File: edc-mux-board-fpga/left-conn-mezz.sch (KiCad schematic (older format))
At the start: 86 parts, among them J13 Device 0, J14 Device 3, J15 Device 1, J16 Device 4, J17 Left Mezzanine Board Connecto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, J18 Left Mezzanine Board Connecto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, J19 Device 2, J20 Device 5

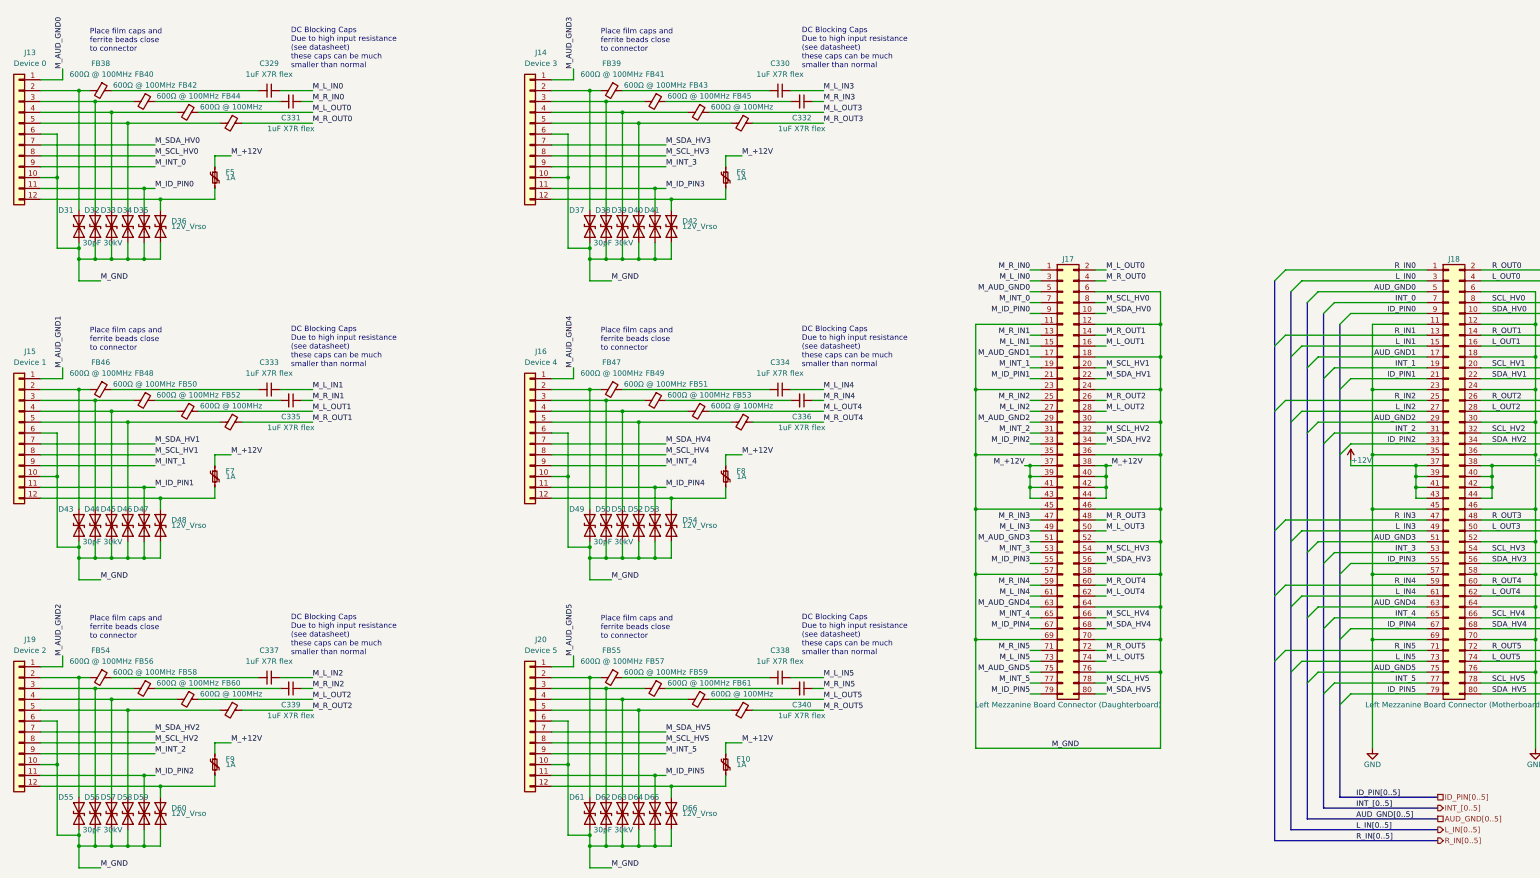
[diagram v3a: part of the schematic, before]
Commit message: re-annotating after adding power ICs and decoupling capacitors.
Also verified most footprints, and updated schematic field data.
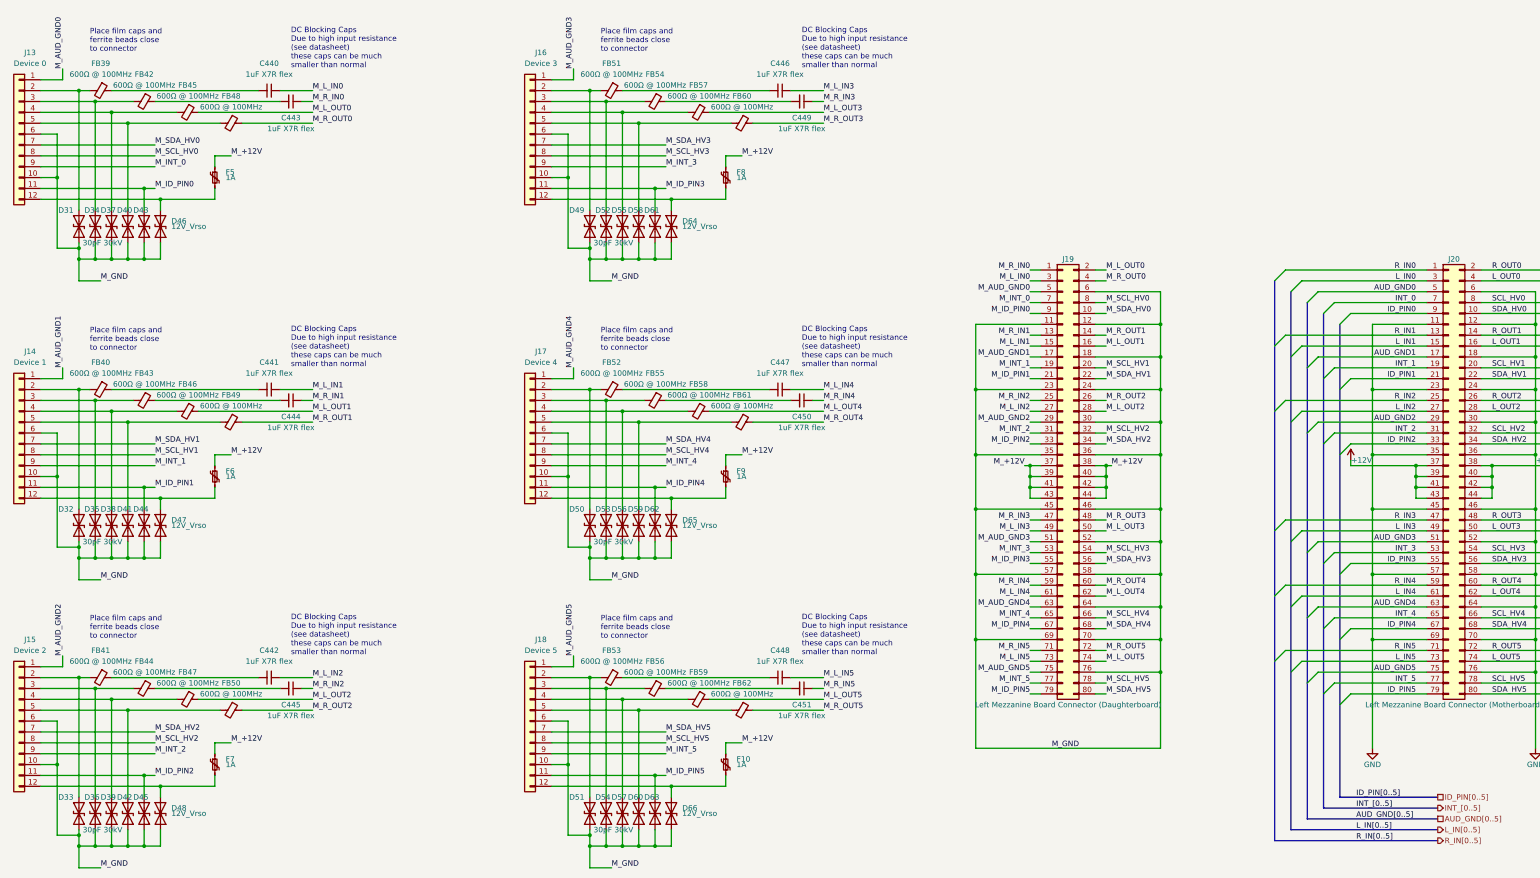
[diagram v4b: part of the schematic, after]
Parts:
- renumbered C329 to C440, C333 to C441, C337 to C442, C331 to C443, C335 to C444, C339 to C445, C330 to C446, C334 to C447, C338 to C448, C332 to C449, C336 to C450, C340 to C451, D43 to D32, D55 to D33, D32 to D34, D44 to D35, D56 to D36, D33 to D37, D45 to D38, D57 to D39, D34 to D40, D46 to D41, D58 to D42, D35 to D43, D47 to D44, D59 to D45, D36 to D46, D48 to D47, D60 to D48, D37 to D49, D49 to D50, D61 to D51, D38 to D52, D50 to D53, D62 to D54, D39 to D55, D51 to D56, D63 to D57, D40 to D58, D52 to D59, D64 to D60, D41 to D61, D53 to D62, D65 to D63, D42 to D64, D54 to D65, F7 to F6, F9 to F7, F6 to F8, F8 to F9, FB38 to FB39, FB46 to FB40, FB54 to FB41, FB40 to FB42, FB48 to FB43, FB56 to FB44, FB42 to FB45, FB50 to FB46, FB58 to FB47, FB44 to FB48, FB52 to FB49, FB60 to FB50, FB39 to FB51, FB47 to FB52, FB55 to FB53, FB41 to FB54, FB49 to FB55, FB57 to FB56, FB43 to FB57, FB51 to FB58, FB45 to FB60, FB53 to FB61, FB61 to FB62, J15 to J14, J19 to J15, J14 to J16, J16 to J17, J20 to J18, J17 to J19, J18 to J20

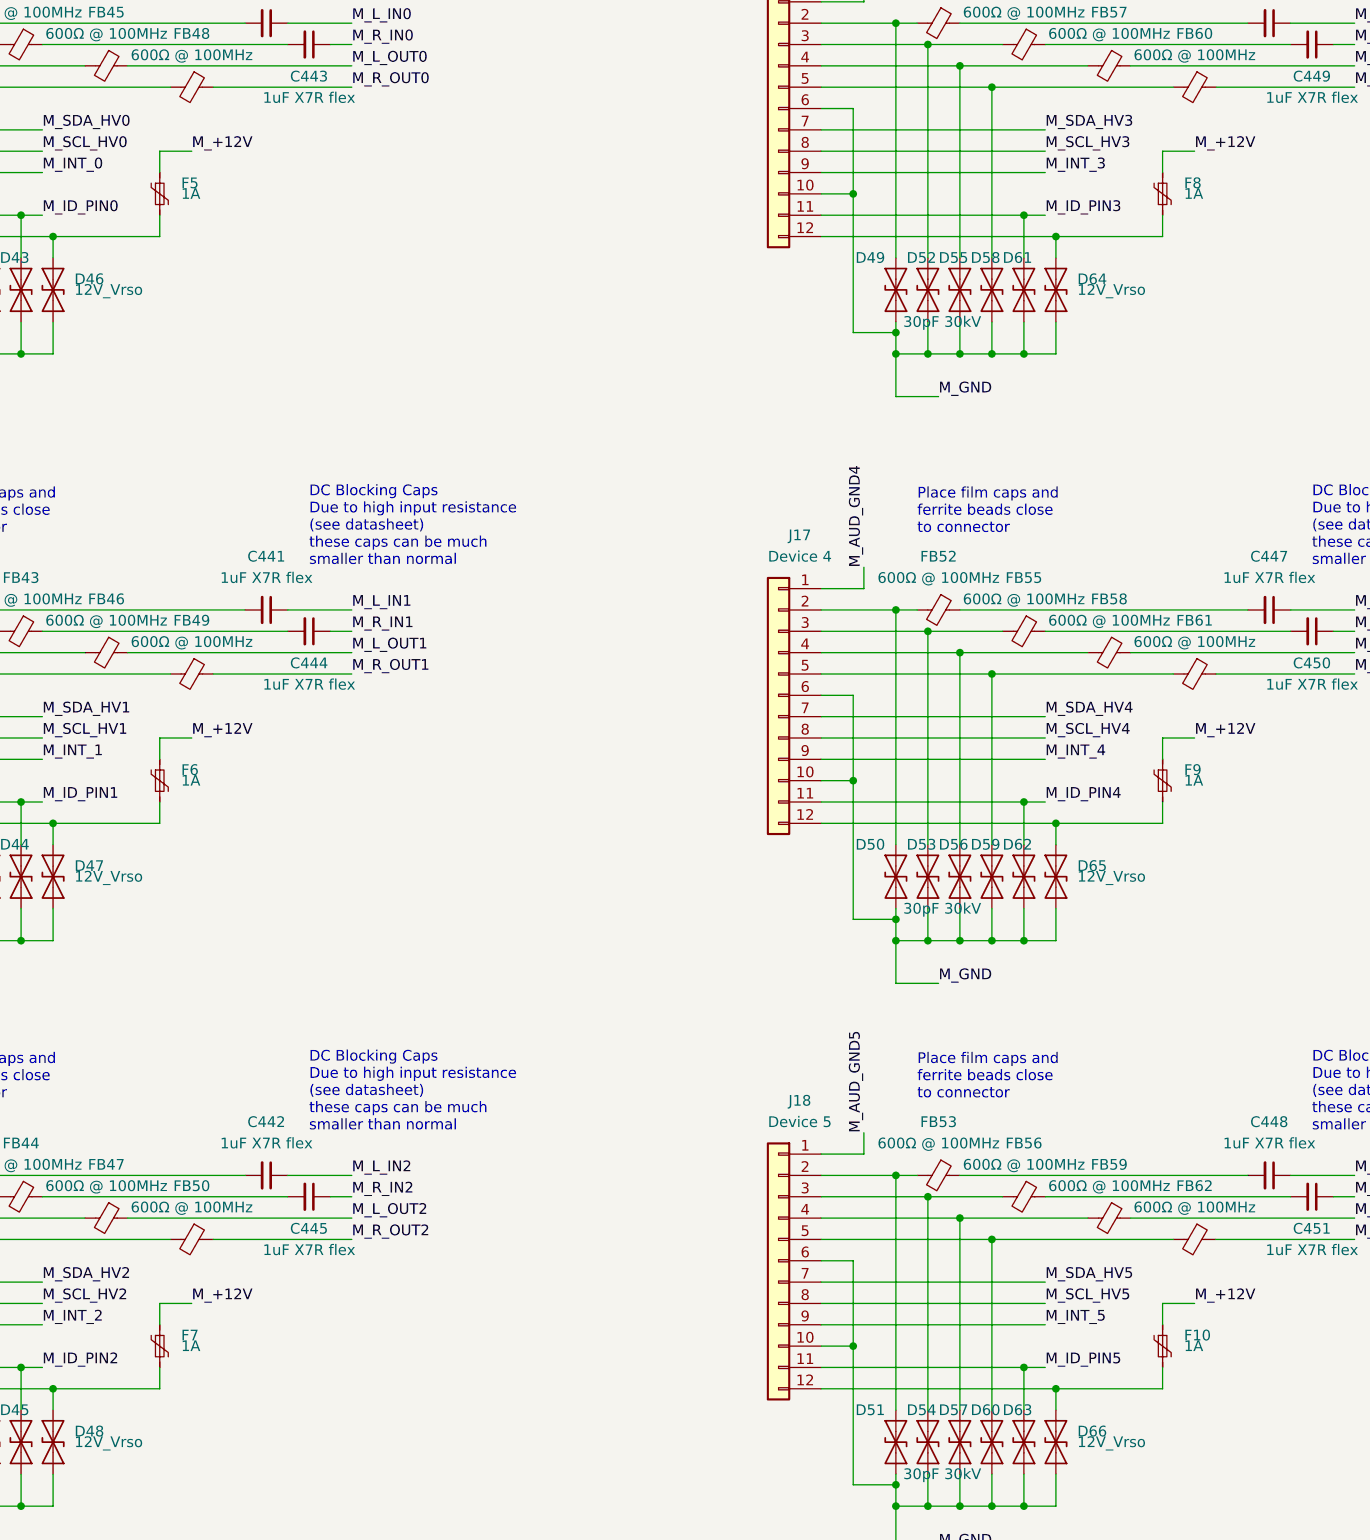
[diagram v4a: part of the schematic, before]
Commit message: removed polyfuses
at the right rating they were going to be too big.
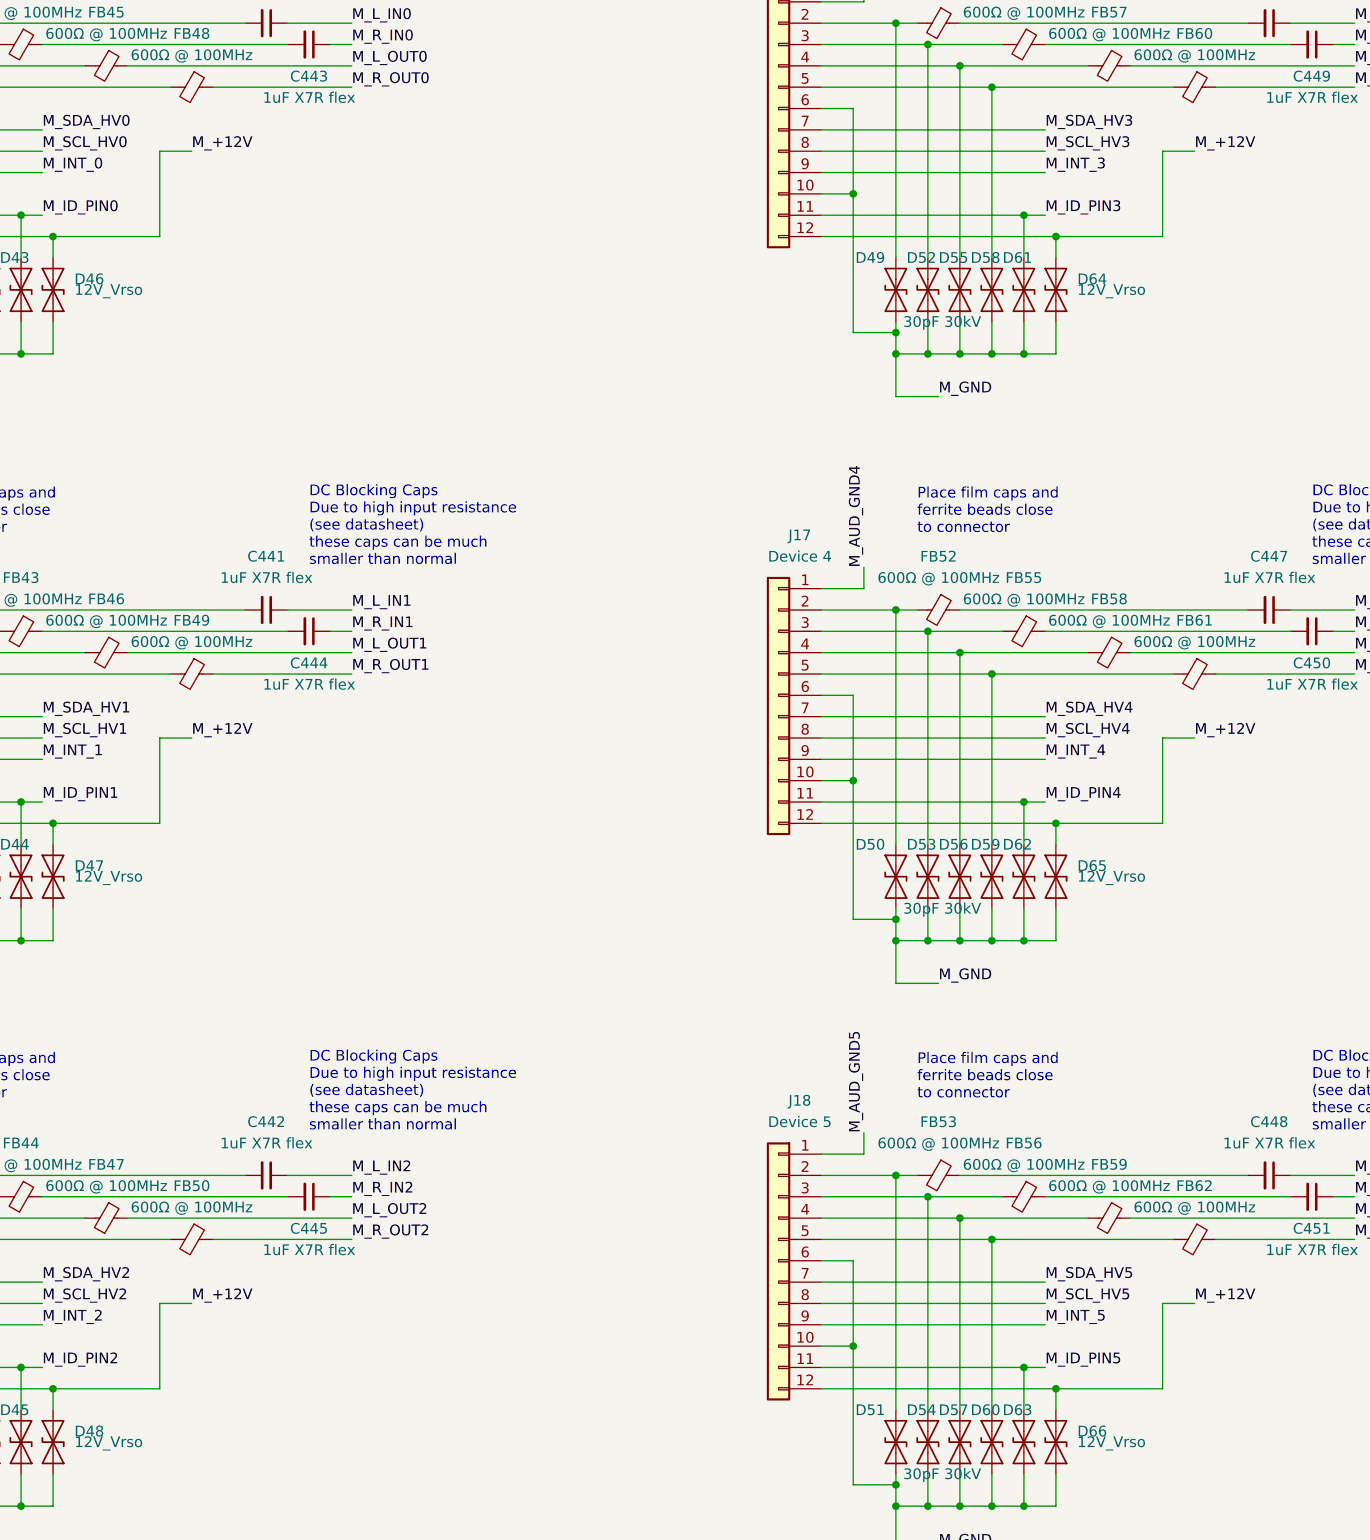
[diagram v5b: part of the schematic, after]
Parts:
- removed F10, F5, F6, F7, F8, F9: 1A, Fuse:Fuse_0603_1608Metric, symbol Device:Polyfuse_Small
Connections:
- net M_+12V: now also D46.1 (A1), D47.1 (A1), D48.1 (A1), D64.1 (A1), D65.1 (A1), D66.1 (A1), J13.12 (Pin_12), J14.12 (Pin_12), J15.12 (Pin_12), J16.12 (Pin_12), J17.12 (Pin_12), J18.12 (Pin_12)
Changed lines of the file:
@@
 Wire Wire Line
 	950  2400 2050 2400
-Wire Wire Line
-	2550 2400 2550 2300
 Text Label 2000 1900 0    50   ~ 0
 M_SDA_HV0
@@
 Text Label 2000 2300 0    50   ~ 0
 M_ID_PIN0
-$Comp
-L Device:Polyfuse_Small F?
-U 1 1 5CC29B23
-P 2550 2200
-AR Path="/5CC6CC1A/5CC6D47B/5CC29B23" Ref="F?"  Part="1"
-AR Path="/5CB02488/5CC29B23" Ref="F?"  Part="1"
-AR Path="/5CBF625C/5CC29B23" Ref="F5"  Part="1"
-F 0 "F5" H 2650 2250 50  0000 L CNN
-F 1 "1A" H 2650 2200 50  0000 L CNN
-F 2 "Fuse:Fuse_0603_1608Metric" H 2600 2000 50  0001 L CNN
-F 3 "~" H 2550 2200 50  0001 C CNN
-F 4 "0603in/1608mm" H 350 -1800 50  0001 C CNN "Package ID"
-	1    2550 2200
-	1    0    0    -1
-$EndComp
 Wire Wire Line
 	2050 2400 2550 2400
-Wire Wire Line
-	2550 2100 2550 2000
 Text Label 1500 3150 0    50   ~ 0
 M_GND
@@
 Wire Wire Line
 	950  5150 2050 5150
-Wire Wire Line
-	2550 5150 2550 5050
 Text Label 2000 4650 0    50   ~ 0
 M_SDA_HV1
@@
 Text Label 2000 5050 0    50   ~ 0
 M_ID_PIN1
-$Comp
-L Device:Polyfuse_Small F?
-U 1 1 5D2B621A
-P 2550 4950
-AR Path="/5CC6CC1A/5CC6D47B/5D2B621A" Ref="F?"  Part="1"
-AR Path="/5CB02488/5D2B621A" Ref="F?"  Part="1"
-AR Path="/5CBF625C/5D2B621A" Ref="F6"  Part="1"
-F 0 "F6" H 2650 5000 50  0000 L CNN
-F 1 "1A" H 2650 4950 50  0000 L CNN
-F 2 "Fuse:Fuse_0603_1608Metric" H 2600 4750 50  0001 L CNN
-F 3 "~" H 2550 4950 50  0001 C CNN
-F 4 "0603in/1608mm" H 350 950 50  0001 C CNN "Package ID"
-	1    2550 4950
-	1    0    0    -1
-$EndComp
 Wire Wire Line
 	2050 5150 2550 5150
-Wire Wire Line
-	2550 4850 2550 4750
 Text Label 1500 5900 0    50   ~ 0
 M_GND
@@
 Wire Wire Line
 	950  7800 2050 7800
-Wire Wire Line
-	2550 7800 2550 7700
 Text Label 2000 7300 0    50   ~ 0
 M_SDA_HV2
@@
 Text Label 2000 7700 0    50   ~ 0
 M_ID_PIN2
-$Comp
-L Device:Polyfuse_Small F?
-U 1 1 5D2CEDEF
-P 2550 7600
-AR Path="/5CC6CC1A/5CC6D47B/5D2CEDEF" Ref="F?"  Part="1"
-AR Path="/5CB02488/5D2CEDEF" Ref="F?"  Part="1"
-AR Path="/5CBF625C/5D2CEDEF" Ref="F7"  Part="1"
-F 0 "F7" H 2650 7650 50  0000 L CNN
-F 1 "1A" H 2650 7600 50  0000 L CNN
-F 2 "Fuse:Fuse_0603_1608Metric" H 2600 7400 50  0001 L CNN
-F 3 "~" H 2550 7600 50  0001 C CNN
-F 4 "0603in/1608mm" H 350 3600 50  0001 C CNN "Package ID"
-	1    2550 7600
-	1    0    0    -1
-$EndComp
 Wire Wire Line
 	2050 7800 2550 7800
-Wire Wire Line
-	2550 7500 2550 7400
 Text Label 1500 8550 0    50   ~ 0
 M_GND
@@
 Wire Wire Line
 	5650 2400 6750 2400
-Wire Wire Line
-	7250 2400 7250 2300
 Text Label 6700 1900 0    50   ~ 0
 M_SDA_HV3
@@
 Text Label 6700 2300 0    50   ~ 0
 M_ID_PIN3
-$Comp
-L Device:Polyfuse_Small F?
-U 1 1 5D2E2341
-P 7250 2200
-AR Path="/5CC6CC1A/5CC6D47B/5D2E2341" Ref="F?"  Part="1"
-AR Path="/5CB02488/5D2E2341" Ref="F?"  Part="1"
-AR Path="/5CBF625C/5D2E2341" Ref="F8"  Part="1"
-F 0 "F8" H 7350 2250 50  0000 L CNN
-F 1 "1A" H 7350 2200 50  0000 L CNN
-F 2 "Fuse:Fuse_0603_1608Metric" H 7300 2000 50  0001 L CNN
-F 3 "~" H 7250 2200 50  0001 C CNN
-F 4 "0603in/1608mm" H 5050 -1800 50  0001 C CNN "Package ID"
-	1    7250 2200
-	1    0    0    -1
-$EndComp
 Wire Wire Line
 	6750 2400 7250 2400
-Wire Wire Line
-	7250 2100 7250 2000
 Text Label 6200 3150 0    50   ~ 0
 M_GND
@@
 Wire Wire Line
 	5650 5150 6750 5150
-Wire Wire Line
-	7250 5150 7250 5050
 Text Label 6700 4650 0    50   ~ 0
 M_SDA_HV4
@@
 Text Label 6700 5050 0    50   ~ 0
 M_ID_PIN4
-$Comp
-L Device:Polyfuse_Small F?
-U 1 1 5D2FA24A
-P 7250 4950
-AR Path="/5CC6CC1A/5CC6D47B/5D2FA24A" Ref="F?"  Part="1"
-AR Path="/5CB02488/5D2FA24A" Ref="F?"  Part="1"
-AR Path="/5CBF625C/5D2FA24A" Ref="F9"  Part="1"
-F 0 "F9" H 7350 5000 50  0000 L CNN
-F 1 "1A" H 7350 4950 50  0000 L CNN
-F 2 "Fuse:Fuse_0603_1608Metric" H 7300 4750 50  0001 L CNN
-F 3 "~" H 7250 4950 50  0001 C CNN
-F 4 "0603in/1608mm" H 5050 950 50  0001 C CNN "Package ID"
-	1    7250 4950
-	1    0    0    -1
-$EndComp
 Wire Wire Line
 	6750 5150 7250 5150
-Wire Wire Line
-	7250 4850 7250 4750
 Text Label 6200 5900 0    50   ~ 0
 M_GND
@@
 Wire Wire Line
 	5650 7800 6750 7800
-Wire Wire Line
-	7250 7800 7250 7700
 Text Label 6700 7300 0    50   ~ 0
 M_SDA_HV5
@@
 Text Label 6700 7700 0    50   ~ 0
 M_ID_PIN5
-$Comp
-L Device:Polyfuse_Small F?
-U 1 1 5D310F81
-P 7250 7600
-AR Path="/5CC6CC1A/5CC6D47B/5D310F81" Ref="F?"  Part="1"
-AR Path="/5CB02488/5D310F81" Ref="F?"  Part="1"
-AR Path="/5CBF625C/5D310F81" Ref="F10"  Part="1"
-F 0 "F10" H 7350 7650 50  0000 L CNN
-F 1 "1A" H 7350 7600 50  0000 L CNN
-F 2 "Fuse:Fuse_0603_1608Metric" H 7300 7400 50  0001 L CNN
-F 3 "~" H 7250 7600 50  0001 C CNN
-F 4 "0603in/1608mm" H 5050 3600 50  0001 C CNN "Package ID"
-	1    7250 7600
-	1    0    0    -1
-$EndComp
 Wire Wire Line
 	6750 7800 7250 7800
-Wire Wire Line
-	7250 7500 7250 7400
 Text Label 6200 8550 0    50   ~ 0
 M_GND
@@
 Wire Wire Line
 	11250 3550 11250 3850
+Wire Wire Line
+	2550 2000 2550 2400
+Wire Wire Line
+	2550 4750 2550 5150
+Wire Wire Line
+	2550 7400 2550 7800
+Wire Wire Line
+	7250 7400 7250 7800
+Wire Wire Line
+	7250 4750 7250 5150
+Wire Wire Line
+	7250 2000 7250 2400
 Wire Bus Line
 	12300 3150 12300 8300
